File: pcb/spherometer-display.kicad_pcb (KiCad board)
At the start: 2 copper layers, 34 x 12.2 mm, 14 parts, among them J1 Battery, J2 Indicator, J3 Disp, J4 Programming, Q1 NPN, Q2 NPN, SW1 UI-Button, U1 ATTINY85V-10SU

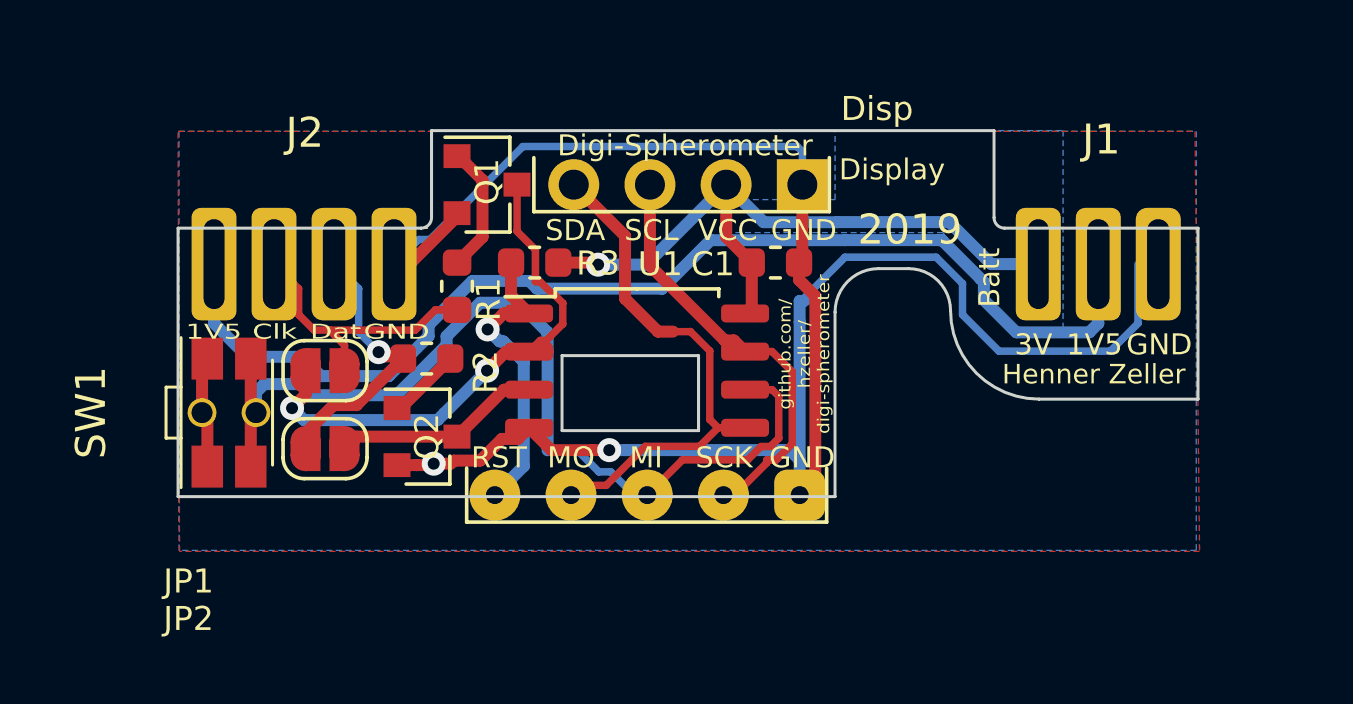
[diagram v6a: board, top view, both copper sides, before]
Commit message: DFM: Add fillets to inner cut-out
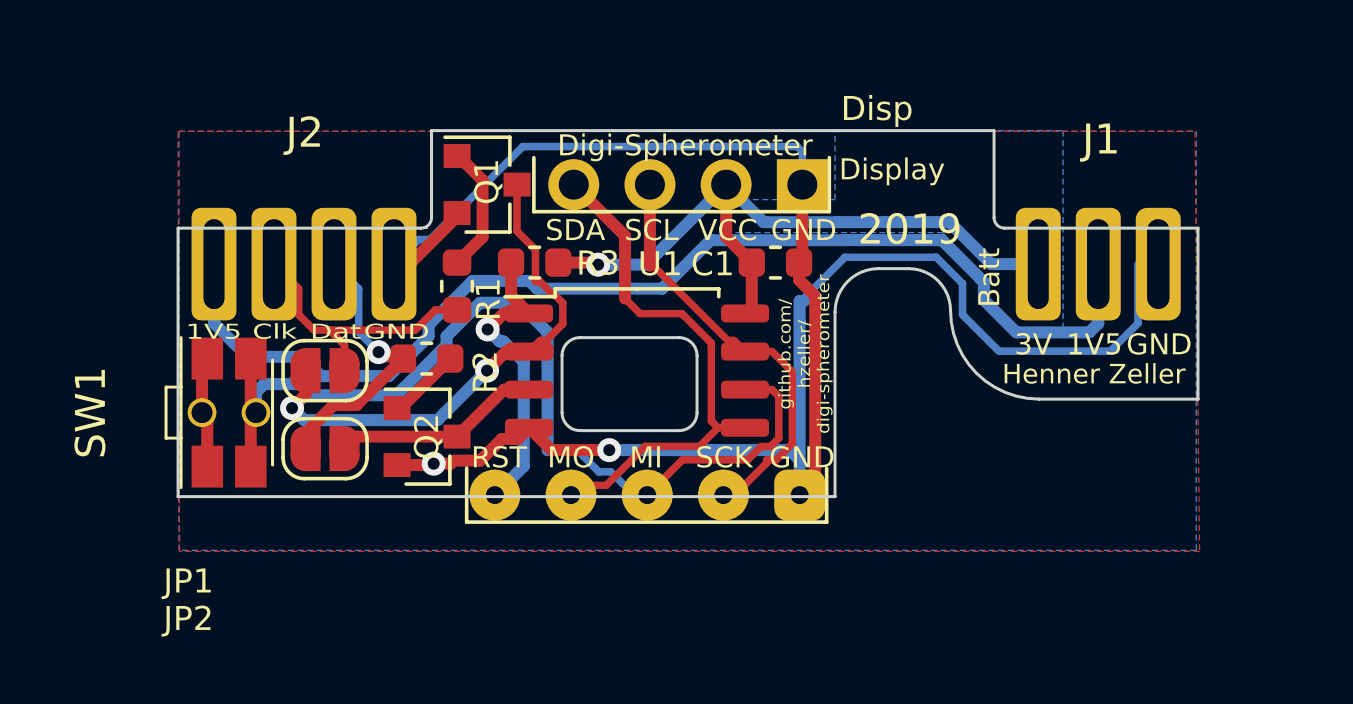
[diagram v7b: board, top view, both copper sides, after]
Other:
- outline, holes or cut-outs redrawn
- board text added: "CUT OUT"
- board text added: "Clearance for OLED components"
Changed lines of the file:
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@@
   (general
     (thickness 0.8)
-    (drawings 51)
+    (drawings 57)
     (tracks 215)
     (zones 0)
@@
   )
   (setup
-    (last_trace_width 0.4)
+    (last_trace_width 0.25)
     (user_trace_width 0.4)
     (trace_clearance 0.2)
@@
     )
   )
+  (gr_text "Clearance for\nOLED components" (at 89.3 66.2 90) (layer Cmts.User)
+    (effects (font (size 0.6 0.6) (thickness 0.1)))
+  )
+  (gr_text "CUT OUT" (at 80.6 65.5) (layer Cmts.User)
+    (effects (font (size 0.6 0.6) (thickness 0.1)))
+  )
+  (gr_line (start 78.3 66.4) (end 78.3 64.5) (layer Edge.Cuts) (width 0.1))
+  (gr_line (start 82.8 64.5) (end 82.8 66.4) (layer Edge.Cuts) (width 0.1))
+  (gr_line (start 82.2 67) (end 78.9 67) (layer Edge.Cuts) (width 0.1))
+  (gr_line (start 78.9 63.9) (end 82.2 63.9) (layer Edge.Cuts) (width 0.1))
+  (gr_arc (start 78.9 66.4) (end 78.3 66.4) (angle -90) (layer Edge.Cuts) (width 0.1))
+  (gr_arc (start 82.2 66.4) (end 82.2 67) (angle -90) (layer Edge.Cuts) (width 0.1))
+  (gr_arc (start 82.2 64.5) (end 82.8 64.5) (angle -90) (layer Edge.Cuts) (width 0.1))
+  (gr_arc (start 78.9 64.5) (end 78.9 63.9) (angle -90) (layer Edge.Cuts) (width 0.1))
   (gr_text Batt (at 92.55 61.9 90) (layer F.SilkS)
     (effects (font (size 0.7 0.7) (thickness 0.1)))
@@
     (effects (font (size 0.5 0.7) (thickness 0.1)))
   )
-  (gr_line (start 82.85 64.5) (end 78.3 64.5) (layer Edge.Cuts) (width 0.1))
-  (gr_line (start 82.85 67) (end 82.85 64.5) (layer Edge.Cuts) (width 0.1))
-  (gr_line (start 78.3 67) (end 82.85 67) (layer Edge.Cuts) (width 0.1))
-  (gr_line (start 78.3 64.5) (end 78.3 67) (layer Edge.Cuts) (width 0.1))
   (gr_arc (start 93.05 59.9) (end 93.05 60.25) (angle 90) (layer Edge.Cuts) (width 0.1))
   (gr_line (start 93.05 60.25) (end 99.5 60.25) (layer Edge.Cuts) (width 0.1))
@@
   (segment (start 77.2 63.095) (end 76.351 63.095) (width 0.4) (layer F.Cu) (net 8))
   (segment (start 83.5 66.905) (end 84.4 66.905) (width 0.25) (layer F.Cu) (net 9))
-  (segment (start 83.5 66.905) (end 83.22501 66.63001) (width 0.25) (layer F.Cu) (net 9))
-  (segment (start 83.22501 66.63001) (end 83.22501 64.344666) (width 0.25) (layer F.Cu) (net 9))
-  (segment (start 83.22501 64.344666) (end 82.580344 63.7) (width 0.25) (layer F.Cu) (net 9))
-  (segment (start 82.580344 63.7) (end 82 63.7) (width 0.25) (layer F.Cu) (net 9))
-  (segment (start 82 63.7) (end 81.5 63.7) (width 0.4) (layer F.Cu) (net 9))
-  (segment (start 81.5 63.7) (end 80.4 62.6) (width 0.4) (layer F.Cu) (net 9))
   (segment (start 80.4 60.511) (end 78.69 58.801) (width 0.4) (layer F.Cu) (net 9))
   (segment (start 80.4 62.6) (end 80.4 60.511) (width 0.4) (layer F.Cu) (net 9))
@@
   (segment (start 81.072334 67.524988) (end 79.772332 68.82499) (width 0.25) (layer F.Cu) (net 9))
   (segment (start 82.880012 67.524988) (end 81.072334 67.524988) (width 0.25) (layer F.Cu) (net 9))
+  (segment (start 83.5 66.905) (end 83.27499 66.67999) (width 0.25) (layer F.Cu) (net 9))
+  (segment (start 83.27499 66.67999) (end 83.27499 64.078168) (width 0.25) (layer F.Cu) (net 9))
+  (segment (start 83.27499 64.078168) (end 82.296822 63.1) (width 0.25) (layer F.Cu) (net 9))
+  (segment (start 80.9 63.1) (end 80.4 62.6) (width 0.25) (layer F.Cu) (net 9))
+  (segment (start 82.296822 63.1) (end 80.9 63.1) (width 0.25) (layer F.Cu) (net 9))
   (segment (start 85.3 64.365) (end 85.97502 65.04002) (width 0.25) (layer F.Cu) (net 10))
   (segment (start 85.97502 65.04002) (end 85.975021 67.438158) (width 0.25) (layer F.Cu) (net 10))
   (segment (start 84.4 64.365) (end 85.3 64.365) (width 0.25) (layer F.Cu) (net 10))
-  (segment (start 84.02929 63.99429) (end 84.4 64.365) (width 0.4) (layer F.Cu) (net 10))
-  (segment (start 83.721456 63.99429) (end 84.02929 63.99429) (width 0.4) (layer F.Cu) (net 10))
-  (segment (start 81.23 61.502834) (end 83.721456 63.99429) (width 0.4) (layer F.Cu) (net 10))
   (segment (start 81.23 58.801) (end 81.23 61.502834) (width 0.4) (layer F.Cu) (net 10))
   (segment (start 85.119979 67.980021) (end 85.433158 67.980021) (width 0.25) (layer F.Cu) (net 10))
@@
   (segment (start 85.119979 67.980021) (end 85.119979 68.080021) (width 0.25) (layer F.Cu) (net 10))
   (segment (start 85.119979 68.080021) (end 84.37501 68.82499) (width 0.25) (layer F.Cu) (net 10))
+  (segment (start 81.336066 61.502834) (end 81.23 61.502834) (width 0.25) (layer F.Cu) (net 10))
+  (segment (start 83.827522 63.99429) (end 81.336066 61.502834) (width 0.25) (layer F.Cu) (net 10))
+  (segment (start 84.02929 63.99429) (end 83.827522 63.99429) (width 0.25) (layer F.Cu) (net 10))
+  (segment (start 84.4 64.365) (end 84.02929 63.99429) (width 0.25) (layer F.Cu) (net 10))
   (segment (start 67.925 64.6) (end 67.925 65.07134) (width 0.4) (layer F.Cu) (net 11))
   (segment (start 67.998647 64.673647) (end 67.998647 64.940437) (width 0.4) (layer F.Cu) (net 11))
